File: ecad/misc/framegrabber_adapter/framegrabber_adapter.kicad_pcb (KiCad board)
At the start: 2 copper layers, 94 x 14 mm, 3 parts, among them J1 IDC 26, J2 MC 1,5/3-G-3.5

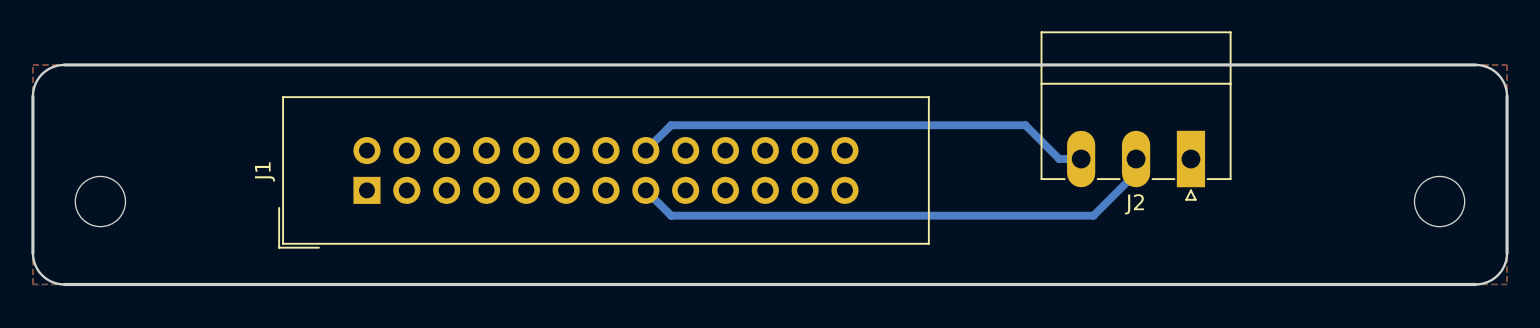
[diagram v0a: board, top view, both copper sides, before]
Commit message: Adds some clearance on the PCI bracket
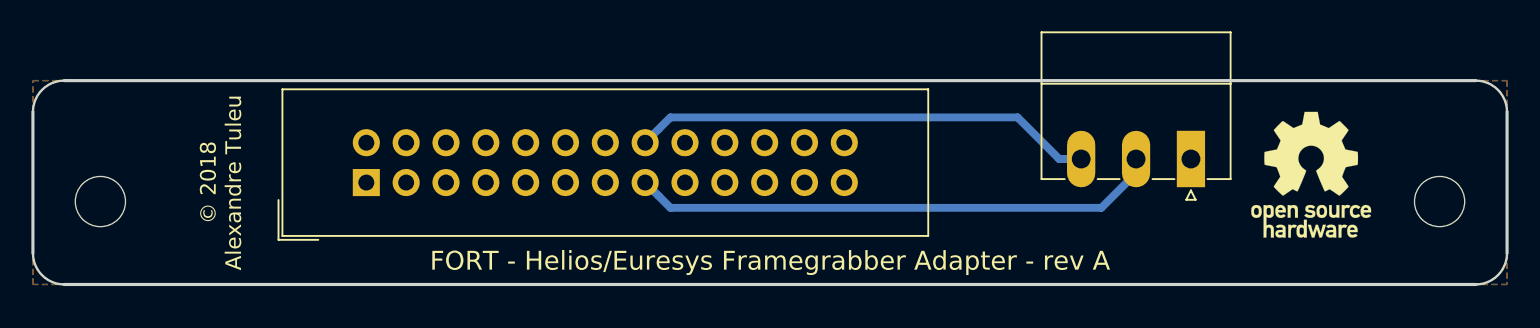
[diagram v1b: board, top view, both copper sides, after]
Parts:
- added REF**: OSHW-Logo_7.5x8mm_SilkScreen, Symbol:OSHW-Logo_7.5x8mm_SilkScreen, F.Cu at (214.5, 72.0)
- moved J1 0.50 mm to (154.3, 72.5)
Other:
- board size 94 x 14 mm -> 94 x 13 mm
- board text added: "FORT - Helios/Euresys Framegrabber Adapter - rev A"
- board text added: "© 2018 Alexandre Tuleu"
